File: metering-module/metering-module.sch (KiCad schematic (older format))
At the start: 38 parts, among them J1 North, J2 South, J3 West, J4 East, Q1 MMBT3904, Q2 MMBT3904, U1 LTV-817S, U2 LTV-817S, U3 BA033CC0FP-E2, U4 MAX3486, U5 MAX3486, U6 MCP23009-E_SS

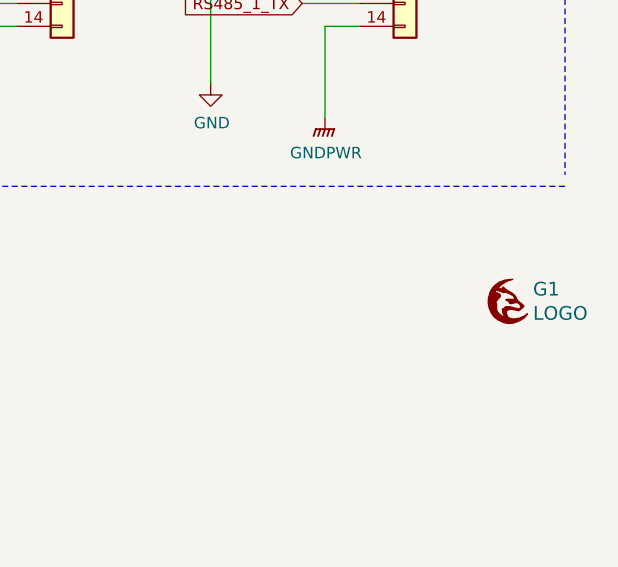
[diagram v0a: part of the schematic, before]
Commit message: Fix too low net clearance
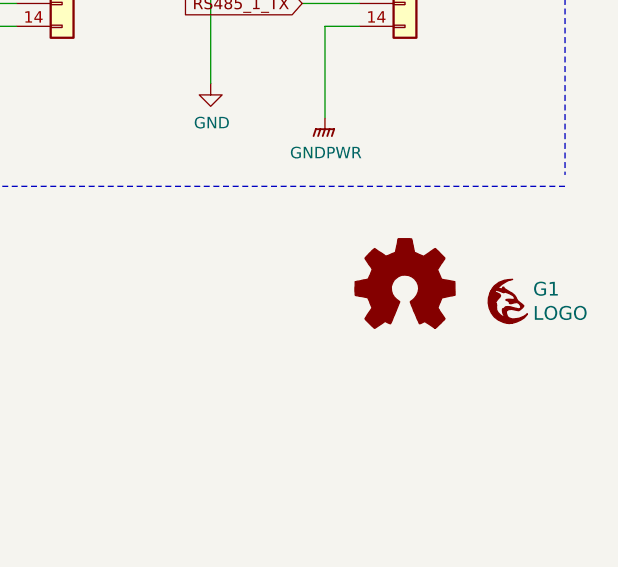
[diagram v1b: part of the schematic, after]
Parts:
- added G2: Logo_Open_Hardware_Small, Symbol:OSHW-Logo2_7.3x6mm_SilkScreen, symbol Graphic:Logo_Open_Hardware_Small
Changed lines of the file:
@@
 	6950 4100 7150 4100
 Connection ~ 6950 4200
+$Comp
+L Graphic:Logo_Open_Hardware_Small G2
+U 1 1 62D8D89B
+P 10250 6250
+F 0 "G2" H 10250 6525 50  0001 C CNN
+F 1 "Logo_Open_Hardware_Small" H 10250 6025 50  0001 C CNN
+F 2 "Symbol:OSHW-Logo2_7.3x6mm_SilkScreen" H 10250 6250 50  0001 C CNN
+F 3 "~" H 10250 6250 50  0001 C CNN
+	1    10250 6250
+	1    0    0    -1
+$EndComp
 $EndSCHEMATC
